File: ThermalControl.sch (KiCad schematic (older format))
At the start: 16 parts, among them U1 ADA4528-2ACPZ-RL, U2 ADA4528-2ACPZ-RL

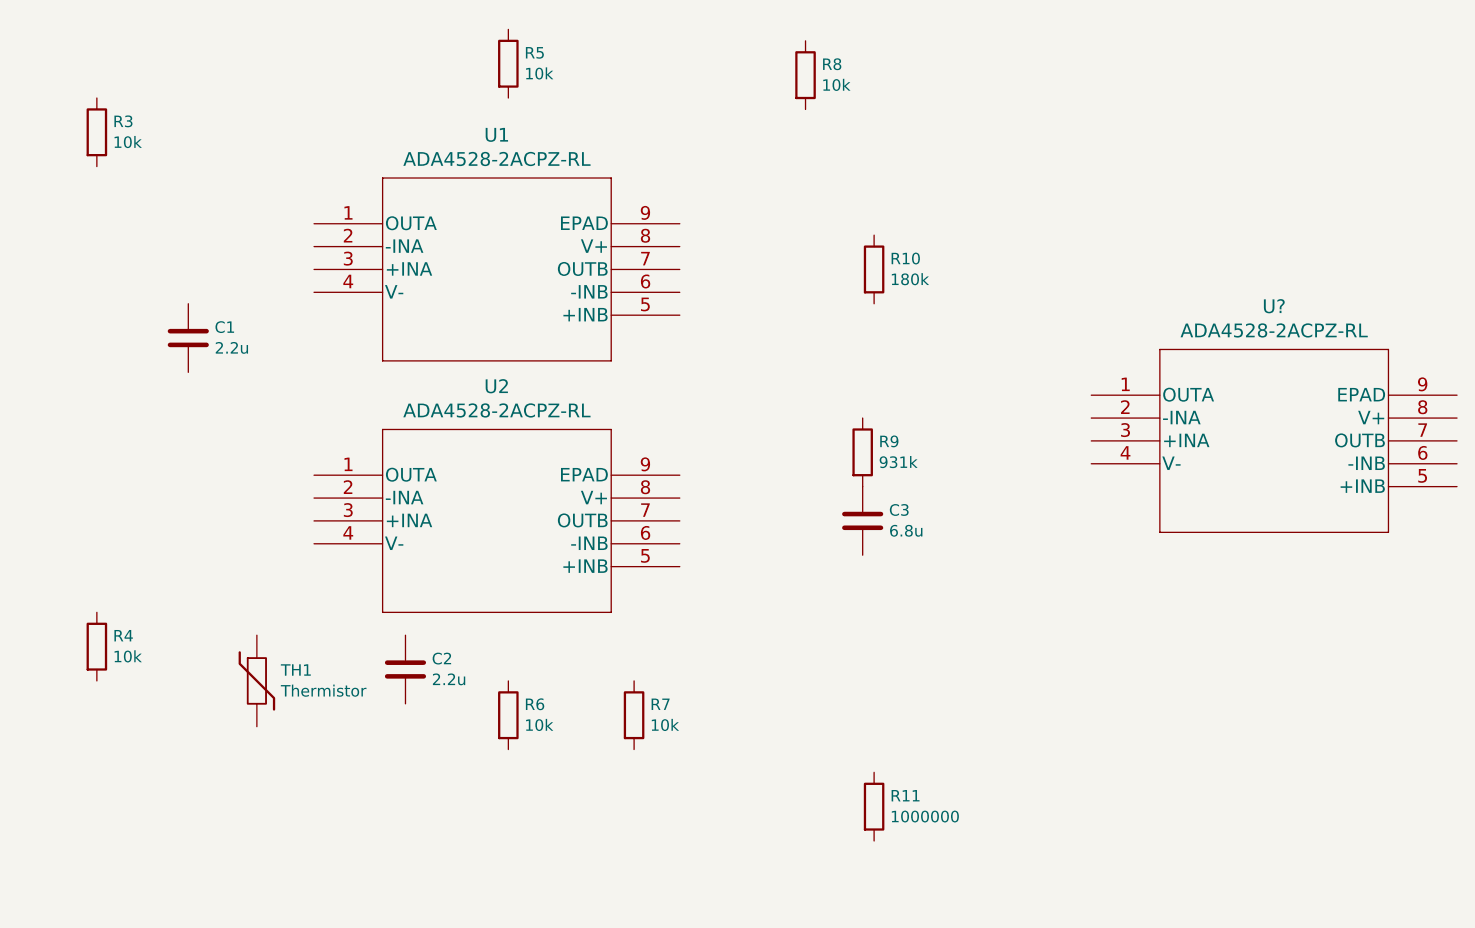
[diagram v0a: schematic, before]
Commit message: added mosfet
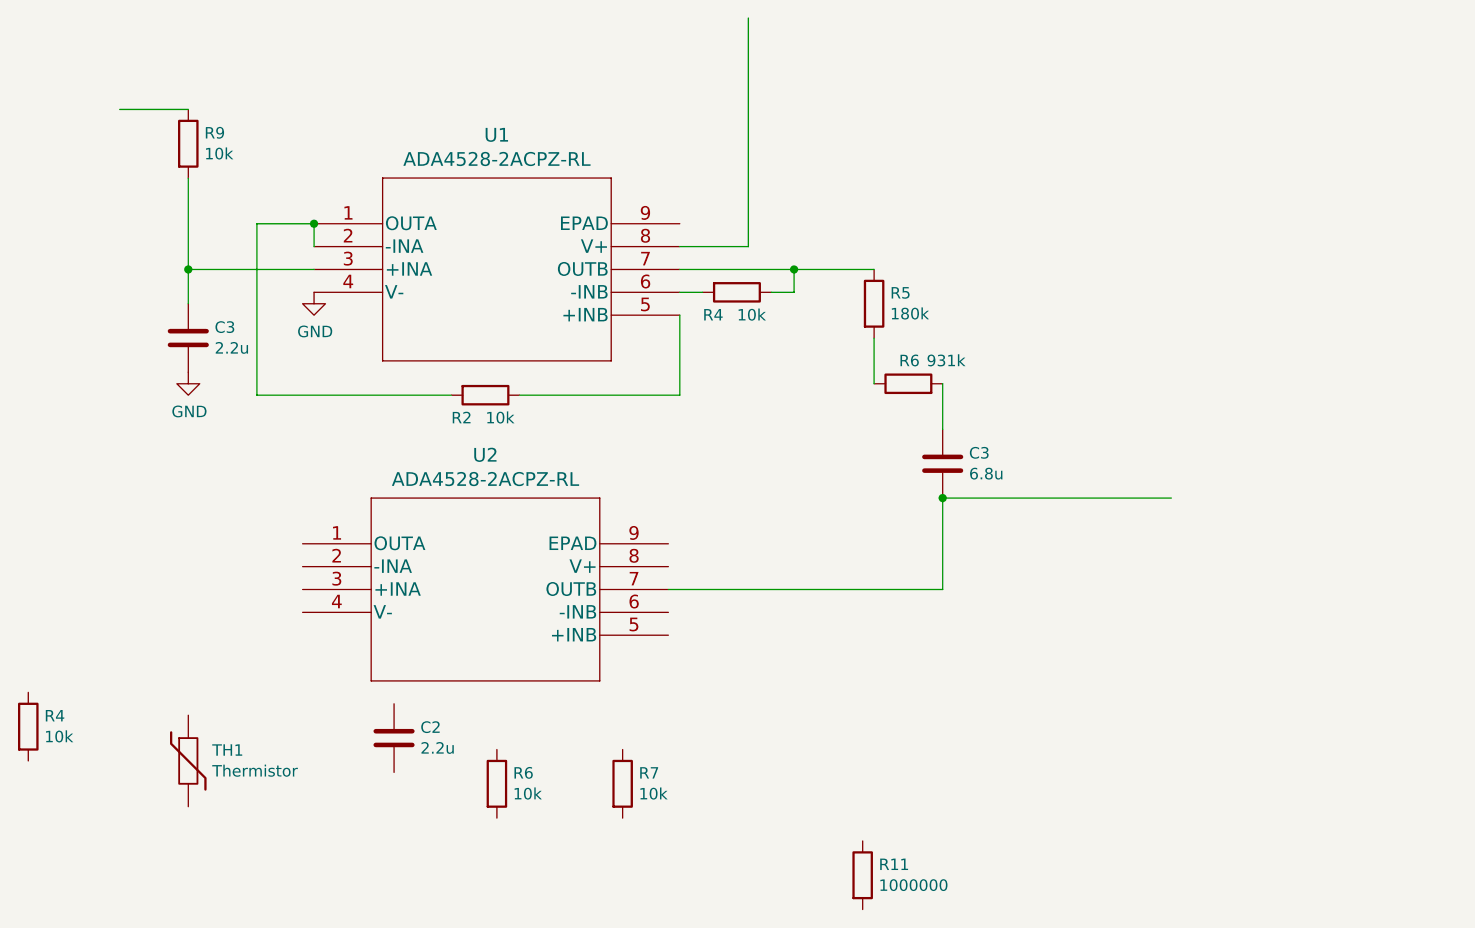
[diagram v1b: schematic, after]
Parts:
- removed U?: ADA4528-2ACPZ-RL, CP_8_11_ADI, symbol 2021-06-09_17-21-09:ADA4528-2ACPZ-RL
- renumbered C1 to C3, R5 to R2, R8 to R4, R10 to R5, R9 to R6, R3 to R9
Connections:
- net labels added: GND
- wire segments 0 -> 22
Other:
- moved on the sheet: C2, C3, R11, R2, R4, R5, R6, R7, R9, TH1, U2

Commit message: add LM4040
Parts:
- U1, U2: symbol 2021-06-09_17-21-09:ADA4528-2ACPZ-RL -> laser-rescue:ADA4528-2ACPZ-RL-2021-06-09_17-21-09
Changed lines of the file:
@@
 $EndDescr
 $Comp
-L 2021-06-09_17-21-09:ADA4528-2ACPZ-RL U1
+L laser-rescue:ADA4528-2ACPZ-RL-2021-06-09_17-21-09 U1
 U 1 1 60C2ACE4
 P 4850 3150
@@
 $EndComp
 $Comp
-L 2021-06-09_17-21-09:ADA4528-2ACPZ-RL U2
+L laser-rescue:ADA4528-2ACPZ-RL-2021-06-09_17-21-09 U2
 U 1 1 60C2B7EB
 P 4800 4550
